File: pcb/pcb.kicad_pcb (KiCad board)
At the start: 2 copper layers, 34 parts, among them J1 Conn_02x08_Odd_Even, J2 B2B-PH-K-S_LF__SN_, Q1 MMUN2211LT1G, SW1 SW_SPST, U1 TPS61090, U2 MCP73871-1AA, X1 USB_C

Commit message: pcb is compiling again
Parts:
- removed X1: USB_C, digikey-footprints:USB-C_Female_E8124-015-01
- added J3: USB_C_Receptacle, digikey-footprints:USB-C_Female_E8124-015-01, F.Cu at (170.2, 95.2)

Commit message: rough positioning of components
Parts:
- moved R13 39.8 mm to (201.4, 95.2), turned to 90 degrees
- moved R9 39.5 mm to (196.9, 91.9)
- moved R10 38.5 mm to (196.9, 90.9), turned to 180 degrees
- moved C6 33.3 mm to (205.2, 89.4)
- moved C3 32.0 mm to (196.3, 95.9), turned to 270 degrees
- moved R15 31.7 mm to (196.8, 93.0), turned to 180 degrees
- moved R12 29.8 mm to (204.5, 92.7)
- moved R6 28.7 mm to (185.0, 105.7), turned to 180 degrees
- moved R11 25.4 mm to (204.4, 91.4)
- moved R2 23.9 mm to (188.3, 111.5)
- moved C5 22.3 mm to (187.8, 103.6)
- moved D2 21.7 mm to (187.9, 106.4), turned to 180 degrees
- moved J2 21.6 mm to (199.9, 83.3), turned to 0 degrees
- moved Q1 21.5 mm to (197.9, 106.3)
- moved L1 20.3 mm to (204.3, 105.8)
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
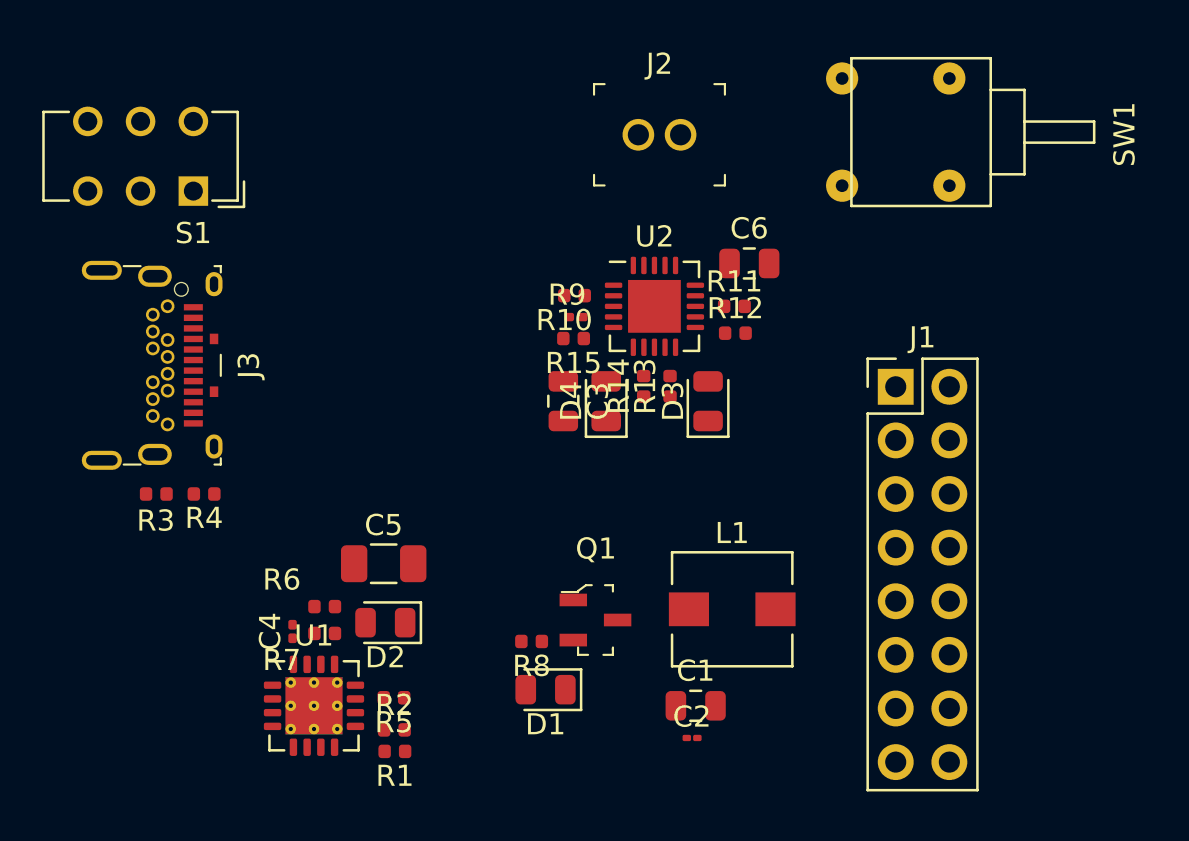
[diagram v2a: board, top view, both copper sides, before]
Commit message: cleaned up layout a little
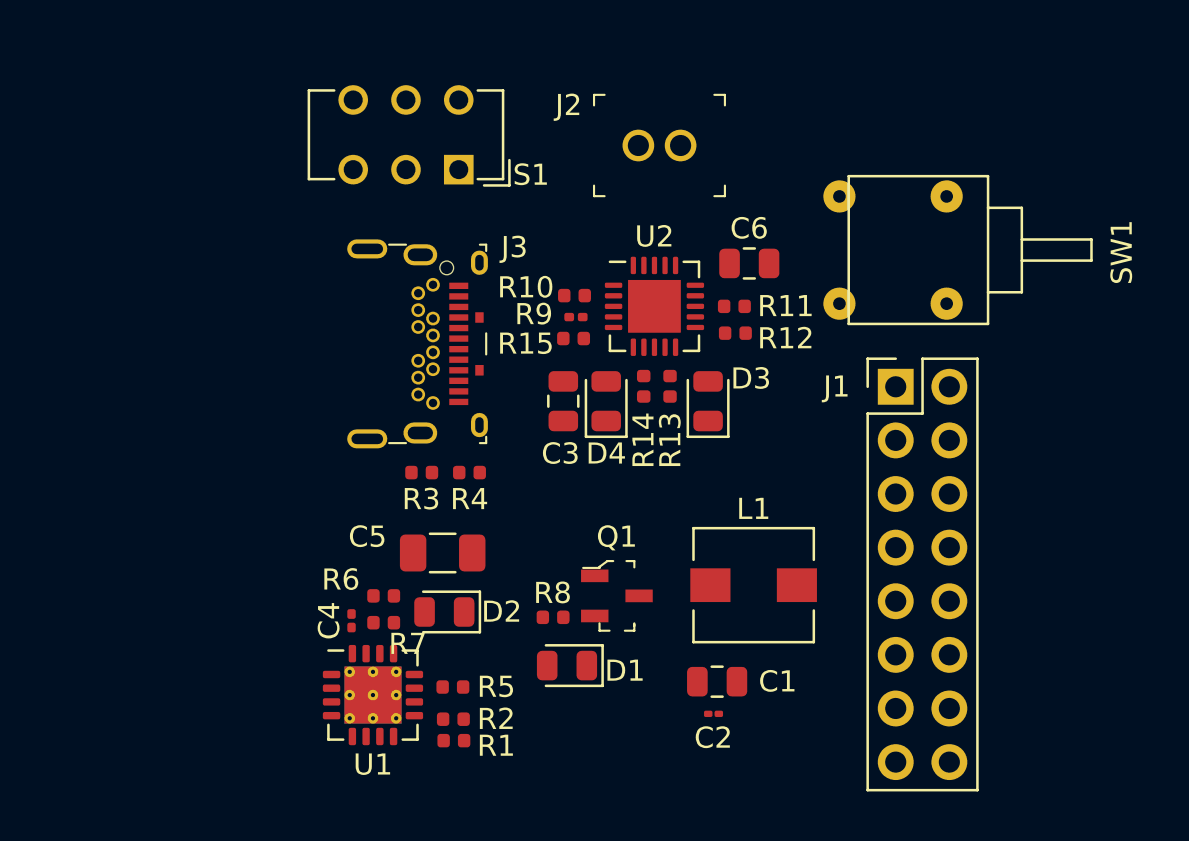
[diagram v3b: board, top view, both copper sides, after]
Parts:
- moved S1 12.6 mm to (191.4, 85.0)
- moved J3 12.6 mm to (191.4, 93.2)
- moved R3 12.6 mm to (189.6, 99.3)
- moved R4 12.6 mm to (191.9, 99.3)
- moved SW1 5.59 mm to (212.0, 88.8)
- moved C4 2.84 mm to (186.3, 106.3)
- moved C5 2.84 mm to (190.6, 103.1)
- moved D2 2.84 mm to (190.7, 105.9)
- moved R6 2.84 mm to (187.8, 105.2)
- moved R7 2.84 mm to (187.8, 106.4)
- moved R1 2.84 mm to (191.2, 112.0)
- moved R2 2.84 mm to (191.1, 111.0)
- moved R5 2.84 mm to (191.1, 109.5)
- moved U1 2.84 mm to (187.3, 109.9)
- moved C1 1.53 mm to (203.6, 109.2)
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
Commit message: in work, PCB layup
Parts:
- moved C1 27.4 mm to (183.4, 90.8), turned to 270 degrees
- moved C2 26.4 mm to (185.0, 91.8), turned to 270 degrees
- moved L1 22.0 mm to (185.2, 96.0), turned to 180 degrees
- moved Q1 21.7 mm to (179.6, 95.2)
- moved R8 20.1 mm to (177.2, 98.9), turned to 270 degrees
- moved D1 19.3 mm to (179.8, 98.9)
- moved R3 15.3 mm to (177.9, 89.4)
- moved R4 15.3 mm to (180.2, 89.4)
- moved C5 12.3 mm to (178.3, 102.9), turned to 90 degrees
- moved J3 11.3 mm to (182.1, 86.7), turned to 180 degrees
- moved R1 10.5 mm to (187.2, 102.3), turned to 270 degrees
- moved D2 10.1 mm to (181.1, 102.8), turned to 270 degrees
- moved R2 9.96 mm to (186.2, 102.4), turned to 90 degrees
- moved R5 9.59 mm to (184.7, 102.4), turned to 270 degrees
- moved C3 8.75 mm to (189.6, 90.3)
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
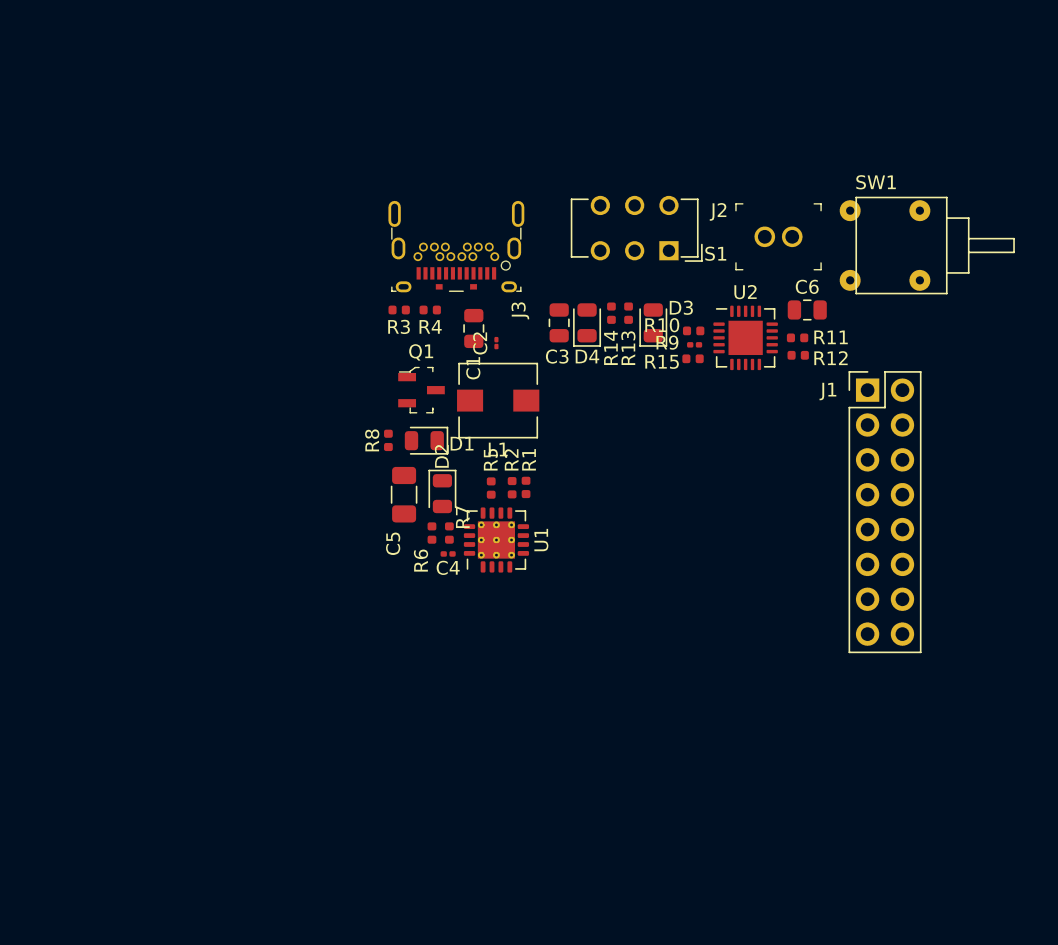
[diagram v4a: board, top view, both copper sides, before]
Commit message: added PCB models
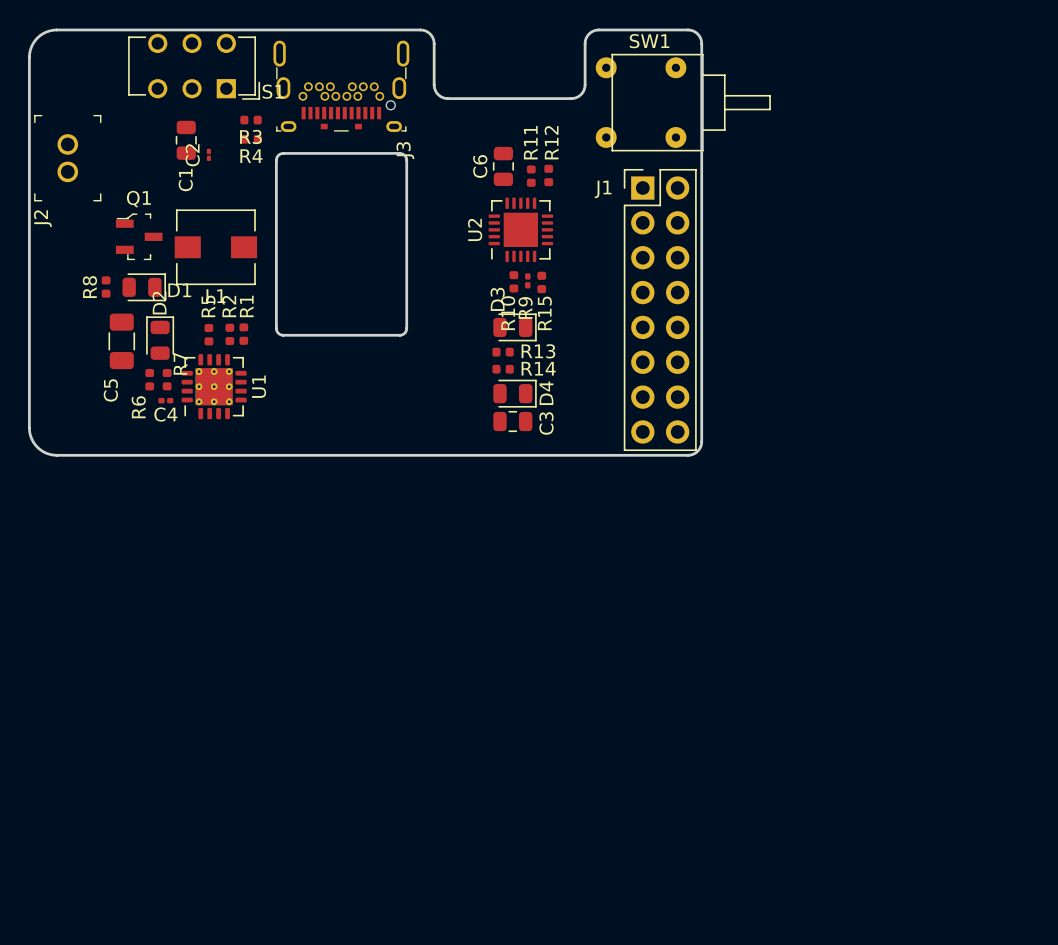
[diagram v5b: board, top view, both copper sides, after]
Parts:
- moved J2 51.0 mm to (153.8, 79.3), turned to 90 degrees
- moved S1 34.4 mm to (165.4, 73.3)
- moved C1 25.0 mm to (162.4, 77.0)
- moved C2 25.0 mm to (164.1, 78.1)
- moved C6 24.5 mm to (185.5, 78.9), turned to 90 degrees
- moved C4 23.4 mm to (160.9, 96.0)
- moved D1 23.4 mm to (159.2, 87.8)
- moved D2 23.4 mm to (160.5, 91.6)
- moved Q1 23.4 mm to (159.0, 84.1)
- moved R1 23.4 mm to (166.6, 91.2)
- moved R6 23.4 mm to (159.8, 94.5)
- moved R7 23.4 mm to (161.0, 94.5)
- moved C5 23.4 mm to (157.7, 91.7)
- moved L1 23.4 mm to (164.6, 84.8)
- moved R5 23.4 mm to (164.1, 91.2)
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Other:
- board outline added: 49 x 31 mm

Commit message: checkin
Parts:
- moved D2 42.8 mm to (197.5, 70.1), turned to 0 degrees
- moved D1 26.0 mm to (181.9, 75.2)
- moved D4 20.7 mm to (190.1, 75.2), turned to 0 degrees
- moved D3 15.5 mm to (186.1, 75.2)
- moved J3 0.76 mm to (173.7, 75.8)
- moved SW1 0.52 mm to (195.5, 74.8)
- moved S1 0.13 mm to (165.2, 73.3)
- moved R14 0.13 mm to (185.5, 93.6)
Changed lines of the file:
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@@
   )
   (module digikey-footprints:USB-C_Female_E8124-015-01 (layer F.Cu)
-    (at 173.736 75.057 180)
+    (at 173.736 75.819 180)
     (descr https://www.digikey.com/product-detail/en/pulse-electronics-network/E8124-015-01/553-3195-2-ND/5800435)
     (attr smd)
-    (fp_text reference J3 (at -4.572 -2.64 270) (layer F.SilkS)
+    (fp_text reference J3 (at -5.969 -1.778) (layer F.SilkS)
       (effects (font (size 1 1) (thickness 0.15)))
     )
@@
   )
   (module LED_SMD:LED_0805_2012Metric (layer F.Cu)
-    (at 159.2095 87.757 180)
+    (at 181.9425 75.184 180)
     (descr "LED SMD 0805 (2012 Metric), square (rectangular) end terminal, IPC_7351 nominal, (Body size source: https://docs.google.com/spreadsheets/d/1BsfQQcO9C6DZCsRaXUlFlo91Tg2WpOkGARC1WS5S8t0/edit?usp=sharing), generated with kicad-footprint-generator")
     (tags diode)
@@
   )
   (module LED_SMD:LED_0805_2012Metric (layer F.Cu)
-    (at 160.528 91.6155 270)
+    (at 197.5335 70.104)
     (descr "LED SMD 0805 (2012 Metric), square (rectangular) end terminal, IPC_7351 nominal, (Body size source: https://docs.google.com/spreadsheets/d/1BsfQQcO9C6DZCsRaXUlFlo91Tg2WpOkGARC1WS5S8t0/edit?usp=sharing), generated with kicad-footprint-generator")
     (tags diode)
     (attr smd)
-    (fp_text reference D2 (at -2.7155 0 90) (layer F.SilkS)
-      (effects (font (size 1 1) (thickness 0.15)))
-    )
-    (fp_text value BLUE_LED (at 0 1.65 90) (layer F.Fab)
+    (fp_text reference D2 (at -2.7155 0) (layer F.SilkS)
+      (effects (font (size 1 1) (thickness 0.15)))
+    )
+    (fp_text value BLUE_LED (at 0 1.65) (layer F.Fab)
       (effects (font (size 1 1) (thickness 0.15)))
     )
@@
     (fp_line (start 1.68 -0.95) (end 1.68 0.95) (layer F.CrtYd) (width 0.05))
     (fp_line (start 1.68 0.95) (end -1.68 0.95) (layer F.CrtYd) (width 0.05))
-    (fp_text user %R (at 0 0 90) (layer F.Fab)
+    (fp_text user %R (at 0 0) (layer F.Fab)
       (effects (font (size 0.5 0.5) (thickness 0.08)))
     )
-    (pad 2 smd roundrect (at 0.9375 0 270) (size 0.975 1.4) (layers F.Cu F.Paste F.Mask) (roundrect_rratio 0.25)
+    (pad 2 smd roundrect (at 0.9375 0) (size 0.975 1.4) (layers F.Cu F.Paste F.Mask) (roundrect_rratio 0.25)
       (net 4 5.0V))
-    (pad 1 smd roundrect (at -0.9375 0 270) (size 0.975 1.4) (layers F.Cu F.Paste F.Mask) (roundrect_rratio 0.25)
+    (pad 1 smd roundrect (at -0.9375 0) (size 0.975 1.4) (layers F.Cu F.Paste F.Mask) (roundrect_rratio 0.25)
       (net 1 GND))
     (model ${KISYS3DMOD}/LED_SMD.3dshapes/LED_0805_2012Metric.wrl
@@
   )
   (module LED_SMD:LED_0805_2012Metric (layer F.Cu)
-    (at 186.2305 90.678 180)
+    (at 186.1335 75.184 180)
     (descr "LED SMD 0805 (2012 Metric), square (rectangular) end terminal, IPC_7351 nominal, (Body size source: https://docs.google.com/spreadsheets/d/1BsfQQcO9C6DZCsRaXUlFlo91Tg2WpOkGARC1WS5S8t0/edit?usp=sharing), generated with kicad-footprint-generator")
     (tags diode)
@@
   )
   (module LED_SMD:LED_0805_2012Metric (layer F.Cu)
-    (at 186.2305 95.504 180)
+    (at 190.0705 75.184)
     (descr "LED SMD 0805 (2012 Metric), square (rectangular) end terminal, IPC_7351 nominal, (Body size source: https://docs.google.com/spreadsheets/d/1BsfQQcO9C6DZCsRaXUlFlo91Tg2WpOkGARC1WS5S8t0/edit?usp=sharing), generated with kicad-footprint-generator")
     (tags diode)
@@
     (fp_line (start 1.68 -0.95) (end 1.68 0.95) (layer F.CrtYd) (width 0.05))
     (fp_line (start 1.68 0.95) (end -1.68 0.95) (layer F.CrtYd) (width 0.05))
-    (fp_text user %R (at 0 0) (layer F.Fab)
+    (fp_text user %R (at 0.0485 0) (layer F.Fab)
       (effects (font (size 0.5 0.5) (thickness 0.08)))
     )
-    (pad 2 smd roundrect (at 0.9375 0 180) (size 0.975 1.4) (layers F.Cu F.Paste F.Mask) (roundrect_rratio 0.25)
+    (pad 2 smd roundrect (at 0.9375 0) (size 0.975 1.4) (layers F.Cu F.Paste F.Mask) (roundrect_rratio 0.25)
       (net 8 "Net-(D4-Pad2)"))
-    (pad 1 smd roundrect (at -0.9375 0 180) (size 0.975 1.4) (layers F.Cu F.Paste F.Mask) (roundrect_rratio 0.25)
+    (pad 1 smd roundrect (at -0.9375 0) (size 0.975 1.4) (layers F.Cu F.Paste F.Mask) (roundrect_rratio 0.25)
       (net 3 VBUS))
     (model ${KISYS3DMOD}/LED_SMD.3dshapes/LED_0805_2012Metric.wrl
@@
       (effects (font (size 1 1) (thickness 0.15)))
     )
-    (fp_text value 1K (at 0 1.17) (layer F.Fab)
+    (fp_text value 1K (at -0.404 1.17) (layer F.Fab)
       (effects (font (size 1 1) (thickness 0.15)))
     )
@@
   )
   (module Resistor_SMD:R_0402_1005Metric (layer F.Cu)
-    (at 185.524 93.726 180)
+    (at 185.524 93.599 180)
     (descr "Resistor SMD 0402 (1005 Metric), square (rectangular) end terminal, IPC_7351 nominal, (Body size source: http://www.tortai-tech.com/upload/download/2011102023233369053.pdf), generated with kicad-footprint-generator")
     (tags resistor)
@@
   )
   (module Button_Switch_THT:SW_CuK_JS202011AQN_DPDT_Angled (layer F.Cu)
-    (at 165.354 73.279 180)
+    (at 165.227 73.279 180)
     (descr "CuK sub miniature slide switch, JS series, DPDT, right angle, http://www.ckswitches.com/media/1422/js.pdf")
     (tags "switch DPDT")
@@
   )
   (module tinycam:FP11SPA1B1TP00 (layer F.Cu)
-    (at 195.58 74.295 270)
-    (fp_text reference SW1 (at -4.445 -0.635) (layer F.SilkS)
-      (effects (font (size 1 1) (thickness 0.15)))
-    )
+    (at 195.453 74.803 270)
+    (fp_text reference SW1 (at 0.127 3.683) (layer F.SilkS)
+      (effects (font (size 1 1) (thickness 0.15)))
+    )
